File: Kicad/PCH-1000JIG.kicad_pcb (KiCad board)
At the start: 2 copper layers, 81.3 x 61 mm, 16 parts

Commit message: Fixed typo in the UDC labels on silkscreen
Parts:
- UDC 11: renamed from UDT 11
- UDC 12: renamed from UDT 12
- UDC 3: renamed from UDT 3
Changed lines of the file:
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@@
     (tags "test point SMD pad")
     (attr exclude_from_pos_files exclude_from_bom)
-    (fp_text reference "UDT 12" (at 0 -1.998) (layer "F.SilkS")
+    (fp_text reference "UDC 12" (at 0 -1.998) (layer "F.SilkS")
         (effects (font (size 1 1) (thickness 0.15)))
     )
@@
     (tags "test point SMD pad")
     (attr exclude_from_pos_files exclude_from_bom)
-    (fp_text reference "UDT 3" (at 0 -1.998) (layer "F.SilkS")
+    (fp_text reference "UDC 3" (at 0 -1.998) (layer "F.SilkS")
         (effects (font (size 1 1) (thickness 0.15)))
     )
@@
     (tags "test point SMD pad")
     (attr exclude_from_pos_files exclude_from_bom)
-    (fp_text reference "UDT 11" (at 0 -1.998) (layer "F.SilkS")
+    (fp_text reference "UDC 11" (at 0 -1.998) (layer "F.SilkS")
         (effects (font (size 1 1) (thickness 0.15)))
     )

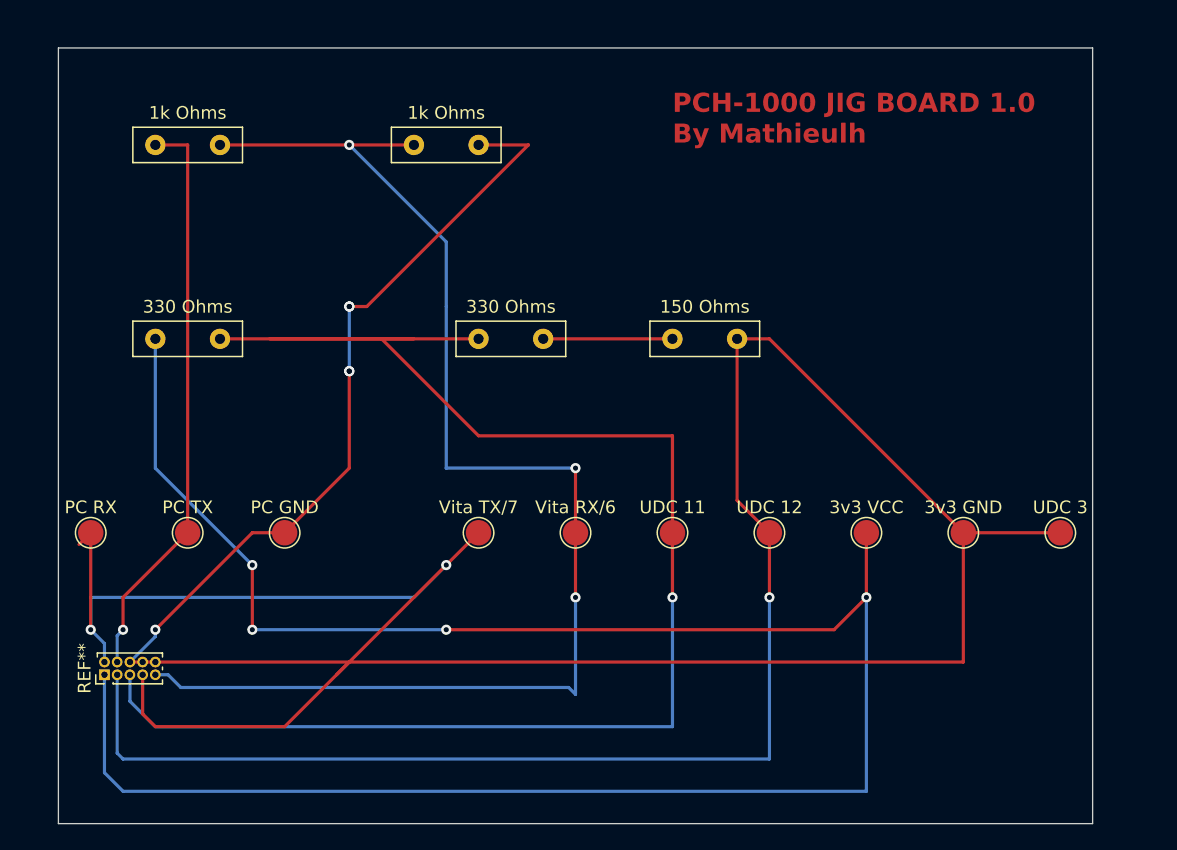
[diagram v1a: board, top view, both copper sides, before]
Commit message: Version 1.1 Fixed implementation fault and increased the footprints size
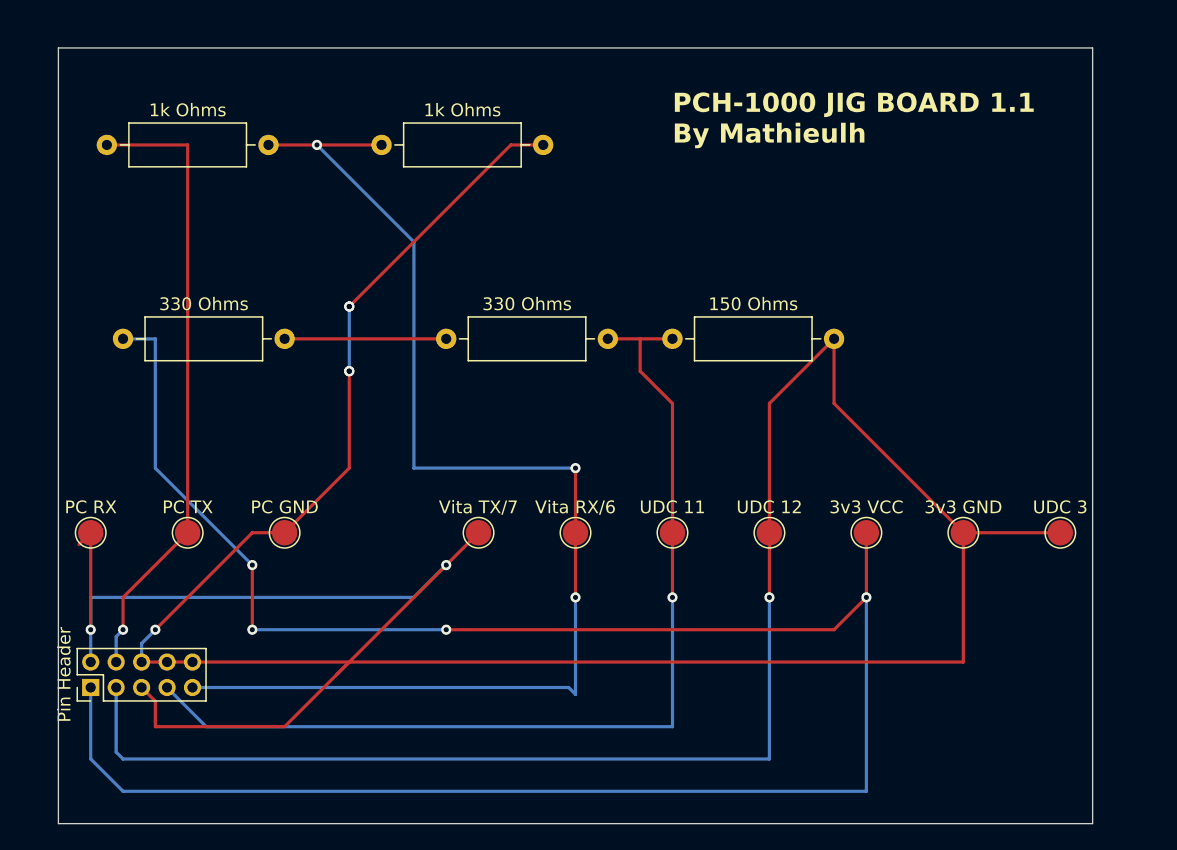
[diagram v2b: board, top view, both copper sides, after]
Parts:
- removed the 150 Ohms at (63.5, 38.1)
- removed the 1k Ohms at (22.9, 22.9)
- removed the 1k Ohms at (43.2, 22.9)
- removed the 330 Ohms at (48.3, 38.1)
- removed the 330 Ohms at (22.9, 38.1)
- removed REF**: PinHeader_2x05_P1.00mm_Vertical, Connector_PinHeader_1.00mm:PinHeader_2x05_P1.00mm_Vertical
- added 150 Ohms: R_Axial_DIN0309_L9.0mm_D3.2mm_P12.70mm_Horizontal, Resistor_THT:R_Axial_DIN0309_L9.0mm_D3.2mm_P12.70mm_Horizontal, F.Cu at (63.5, 38.1)
- added 1k Ohms: R_Axial_DIN0309_L9.0mm_D3.2mm_P12.70mm_Horizontal, Resistor_THT:R_Axial_DIN0309_L9.0mm_D3.2mm_P12.70mm_Horizontal, F.Cu at (19.1, 22.9)
- added 1k Ohms: R_Axial_DIN0309_L9.0mm_D3.2mm_P12.70mm_Horizontal, Resistor_THT:R_Axial_DIN0309_L9.0mm_D3.2mm_P12.70mm_Horizontal, F.Cu at (40.6, 22.9)
- added 330 Ohms: R_Axial_DIN0309_L9.0mm_D3.2mm_P12.70mm_Horizontal, Resistor_THT:R_Axial_DIN0309_L9.0mm_D3.2mm_P12.70mm_Horizontal, F.Cu at (20.3, 38.1)
- added 330 Ohms: R_Axial_DIN0309_L9.0mm_D3.2mm_P12.70mm_Horizontal, Resistor_THT:R_Axial_DIN0309_L9.0mm_D3.2mm_P12.70mm_Horizontal, F.Cu at (45.7, 38.1)
- added Pin Header: PinHeader_2x05_P2.00mm_Vertical, Connector_PinHeader_2.00mm:PinHeader_2x05_P2.00mm_Vertical, F.Cu at (17.8, 65.5)
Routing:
- net (no net): track 790.9 -> 733.6 mm
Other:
- board text added: "PCH-1000 JIG BOARD 1.1 By Mathieulh"
- board text removed: "PCH-1000 JIG BOARD 1.0 By Mathieulh"

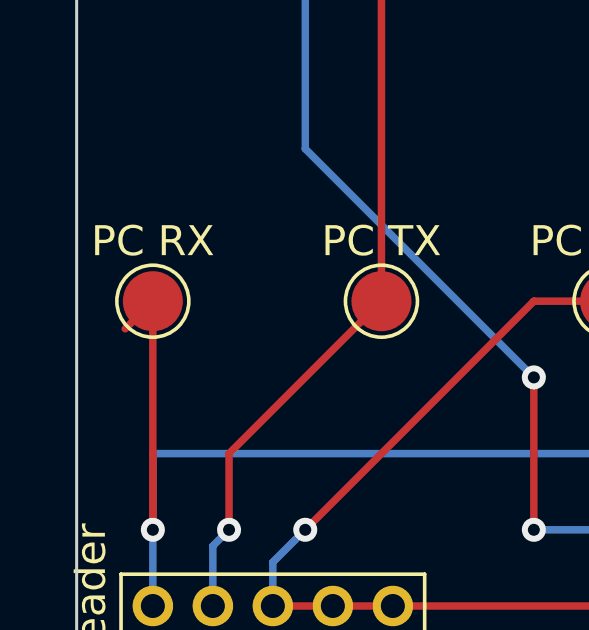
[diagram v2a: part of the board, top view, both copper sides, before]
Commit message: I removed a small leftover trace (which isn't connected to anything)
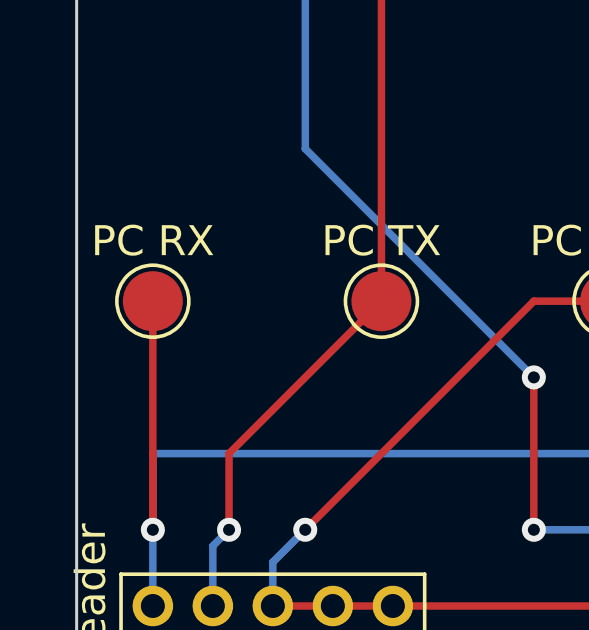
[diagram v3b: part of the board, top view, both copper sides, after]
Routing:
- net (no net): track 733.6 -> 732.3 mm
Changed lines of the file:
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@@
   (segment (start 60.96 40.64) (end 60.96 38.1) (width 0.25) (layer "F.Cu") (net 0))
   (segment (start 25.4 53.34) (end 25.4 22.86) (width 0.25) (layer "F.Cu") (net 0))
-  (segment (start 16.86 54.26) (end 17.78 53.34) (width 0.25) (layer "F.Cu") (net 0))
   (segment (start 25.4 22.86) (end 19.05 22.86) (width 0.25) (layer "F.Cu") (net 0))
   (segment (start 22.86 60.96) (end 30.48 53.34) (width 0.25) (layer "F.Cu") (net 0))

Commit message: Fixed potential design issue on the throughhole board.
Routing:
- net (no net): track 732.3 -> 715.6 mm
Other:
- board size 81.3 x 61 mm -> 83.8 x 61 mm
- board text added: "PCH-1000 JIG BOARD 1.2 By Mathieulh"
- board text removed: "PCH-1000 JIG BOARD 1.1 By Mathieulh"
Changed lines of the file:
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@@
     )
   )
-  (gr_rect (start 15.24 15.24) (end 96.52 76.2)
+  (gr_rect (start 12.7 15.24) (end 96.52 76.2)
     (stroke (width 0.1) (type default)) (fill none) (layer "Edge.Cuts"))
-  (gr_text "PCH-1000 JIG BOARD 1.1\nBy Mathieulh" (at 63.5 22.86) (layer "F.SilkS")
+  (gr_text "PCH-1000 JIG BOARD 1.2\nBy Mathieulh" (at 63.5 22.86) (layer "F.SilkS")
     (effects (font (size 1.5 1.5) (thickness 0.3) bold) (justify left bottom))
   )
   (segment (start 33.02 53.34) (end 38.1 48.26) (width 0.25) (layer "F.Cu") (net 0))
   (segment (start 50.8 22.86) (end 53.34 22.86) (width 0.25) (layer "F.Cu") (net 0))
+  (segment (start 15.365 68.58) (end 18.7 68.58) (width 0.25) (layer "F.Cu") (net 0))
   (segment (start 86.36 53.34) (end 93.98 53.34) (width 0.25) (layer "F.Cu") (net 0))
   (segment (start 17.78 58.42) (end 17.78 53.34) (width 0.25) (layer "F.Cu") (net 0))
@@
   (segment (start 38.1 48.26) (end 38.1 40.64) (width 0.25) (layer "F.Cu") (net 0))
   (segment (start 71.12 58.42) (end 71.12 53.34) (width 0.25) (layer "F.Cu") (net 0))
-  (segment (start 22.86 68.58) (end 22.86 66.58) (width 0.25) (layer "F.Cu") (net 0))
+  (segment (start 17.78 60.96) (end 15.365 63.375) (width 0.25) (layer "F.Cu") (net 0))
   (segment (start 38.1 35.56) (end 50.8 22.86) (width 0.25) (layer "F.Cu") (net 0))
   (segment (start 20.32 60.96) (end 20.32 58.42) (width 0.25) (layer "F.Cu") (net 0))
+  (segment (start 15.365 63.375) (end 15.365 68.58) (width 0.25) (layer "F.Cu") (net 0))
   (segment (start 35.56 22.86) (end 31.75 22.86) (width 0.25) (layer "F.Cu") (net 0))
-  (segment (start 37.1 64.5) (end 45.72 55.88) (width 0.25) (layer "F.Cu") (net 0))
   (segment (start 30.48 53.34) (end 33.02 53.34) (width 0.25) (layer "F.Cu") (net 0))
   (segment (start 17.78 60.96) (end 17.78 58.42) (width 0.25) (layer "F.Cu") (net 0))
   (segment (start 63.5 38.1) (end 60.96 38.1) (width 0.25) (layer "F.Cu") (net 0))
   (segment (start 45.72 55.88) (end 48.26 53.34) (width 0.25) (layer "F.Cu") (net 0))
+  (segment (start 18.7 68.58) (end 21.78 65.5) (width 0.25) (layer "F.Cu") (net 0))
   (segment (start 33.02 38.1) (end 45.72 38.1) (width 0.25) (layer "F.Cu") (net 0))
-  (segment (start 22.86 68.58) (end 33.02 68.58) (width 0.25) (layer "F.Cu") (net 0))
   (segment (start 86.36 63.5) (end 86.36 53.34) (width 0.25) (layer "F.Cu") (net 0))
   (segment (start 78.74 58.42) (end 76.2 60.96) (width 0.25) (layer "F.Cu") (net 0))
-  (segment (start 22.86 66.58) (end 21.78 65.5) (width 0.25) (layer "F.Cu") (net 0))
   (segment (start 30.48 60.96) (end 30.48 55.88) (width 0.25) (layer "F.Cu") (net 0))
   (segment (start 58.42 38.1) (end 60.96 38.1) (width 0.25) (layer "F.Cu") (net 0))
@@
   (segment (start 63.5 58.42) (end 63.5 53.34) (width 0.25) (layer "F.Cu") (net 0))
   (segment (start 76.2 60.96) (end 45.72 60.96) (width 0.25) (layer "F.Cu") (net 0))
-  (segment (start 33.02 68.58) (end 38.1 63.5) (width 0.25) (layer "F.Cu") (net 0))
   (segment (start 60.96 40.64) (end 60.96 38.1) (width 0.25) (layer "F.Cu") (net 0))
   (segment (start 25.4 53.34) (end 25.4 22.86) (width 0.25) (layer "F.Cu") (net 0))

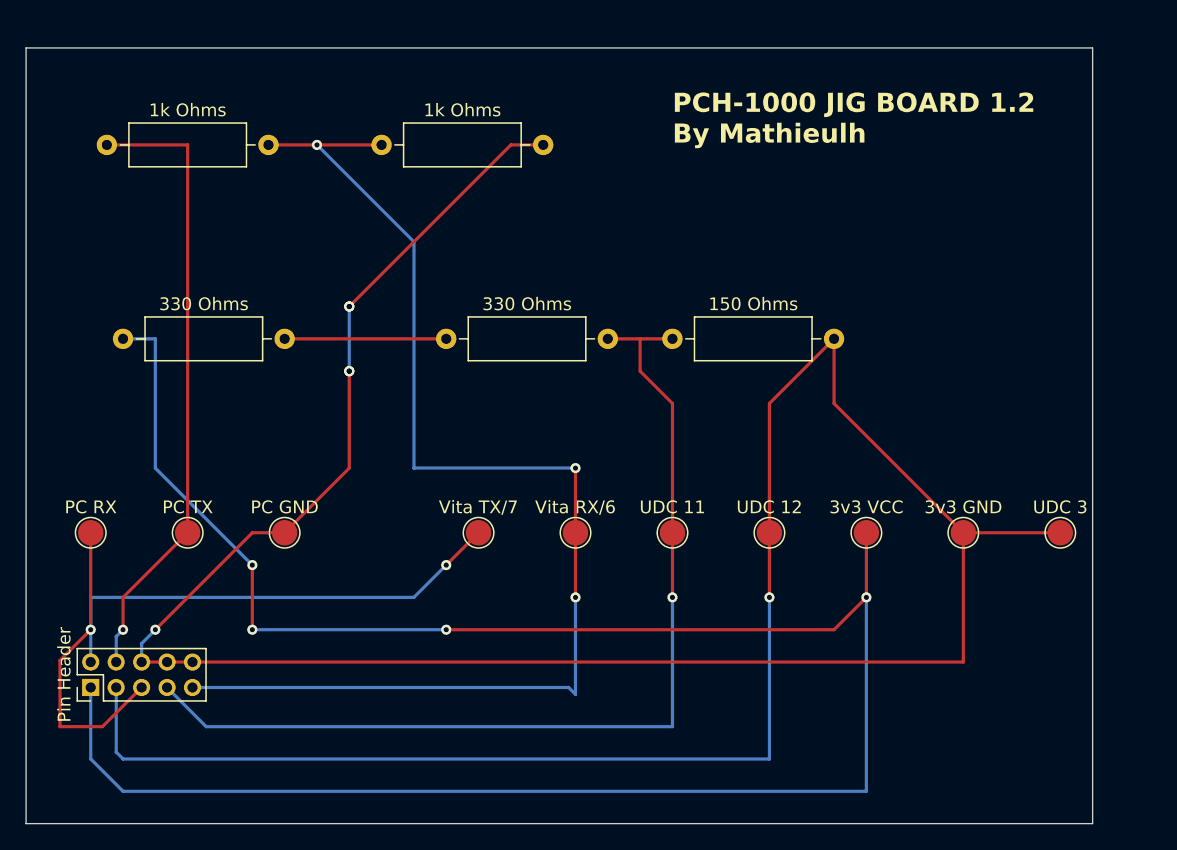
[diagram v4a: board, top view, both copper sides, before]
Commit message: Design slightly off center (fix)
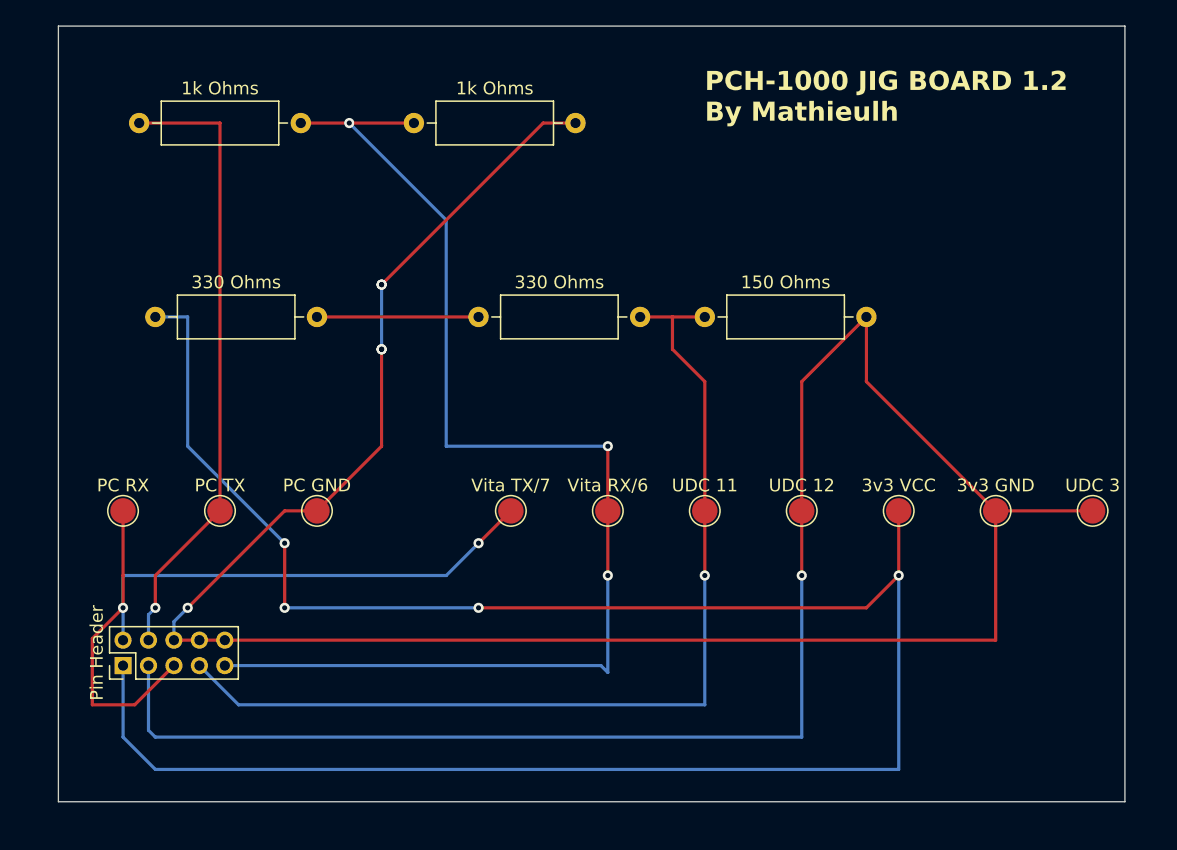
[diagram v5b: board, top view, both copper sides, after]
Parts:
- moved 3v3 GND 3.07 mm to (88.9, 51.6)
- moved 3v3 VCC 3.07 mm to (81.3, 51.6)
- moved UDC 11 3.07 mm to (66.0, 51.6)
- moved PC TX 3.07 mm to (27.9, 51.6)
- moved 150 Ohms 3.07 mm to (66.0, 36.4)
- moved PC GND 3.07 mm to (35.6, 51.6)
- moved PC RX 3.07 mm to (20.3, 51.6)
- moved Vita RX/6 3.07 mm to (58.4, 51.6)
- moved Vita TX/7 3.07 mm to (50.8, 51.6)
- moved 1k Ohms 3.07 mm to (21.6, 21.1)
- moved 1k Ohms 3.07 mm to (43.2, 21.1)
- moved 330 Ohms 3.07 mm to (22.9, 36.4)
- moved 330 Ohms 3.07 mm to (48.3, 36.4)
- moved Pin Header 3.07 mm to (20.3, 63.8)
- moved UDC 12 3.07 mm to (73.7, 51.6)
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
